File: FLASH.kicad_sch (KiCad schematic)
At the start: 0 parts

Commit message: added Buzzer, status LEDs
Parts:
- added C29: 100nF, Capacitor_SMD:C_0603_1608Metric, symbol Device:C
- added R12, R13, R14: 10k, Resistor_SMD:R_0603_1608Metric, symbol Device:R
- added U10: W25Q128JVSIQ, Package_SO:SOIC-8_5.3x5.3mm_P1.27mm, symbol Memory_Flash:W25Q128JVS
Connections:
- new net: R14.2, U10.3 (~{WP}/IO_{2})
- new net: R13.2, U10.7 (~{HOLD}/~{RESET}/IO_{3})
- new net 3V3: C29.1, R12.1, R13.1, R14.1, U10.8 (VCC)
- new net CLK_FLASH: U10.6 (CLK)
- new net CS_FLASH: R12.2, U10.1 (~{CS})
- new net DI_FLASH: U10.5 (DI/IO_{0})
- new net DO_FLASH: U10.2 (DO/IO_{1})
- new net GND: C29.2, U10.4 (GND)

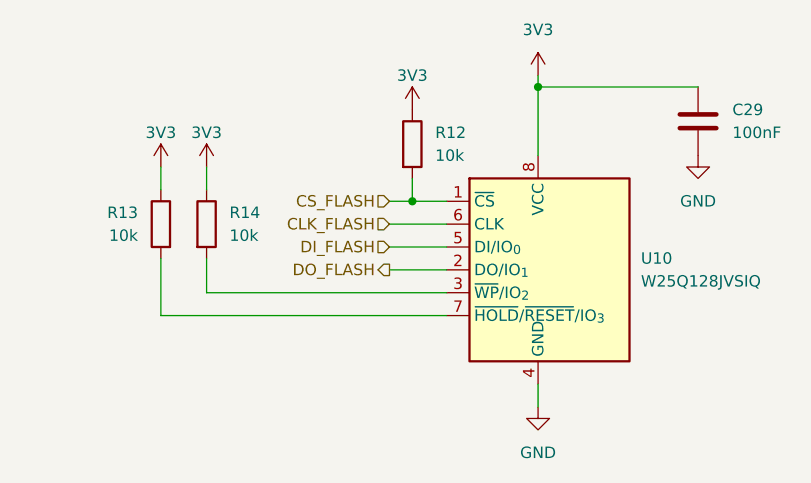
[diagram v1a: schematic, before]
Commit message: Battery protection, camera switch, 64MB flash, ERC clean
- Fuse + TVS on battery input, camera load switch (TPS22917)
- Flash to W25Q512JVFIQ (SOIC-16), hand-solder passive footprints
- Power LED, title blocks, U5 footprint, PWR/NC flags (0 ERC)
- Regenerated schematic PDF
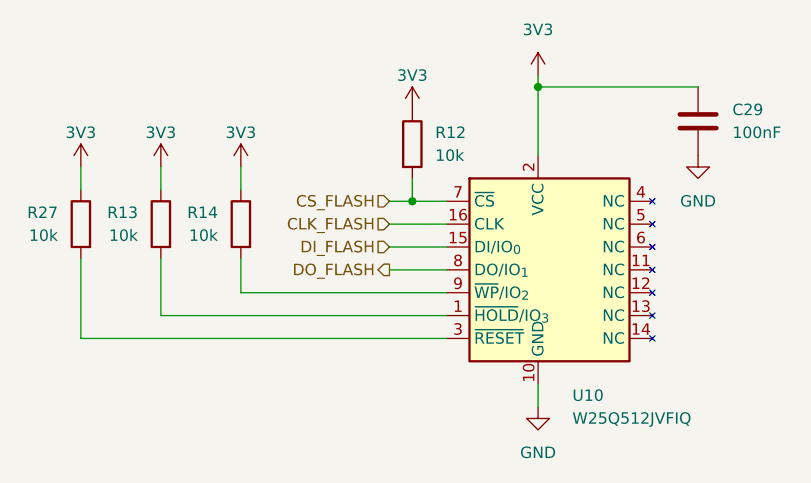
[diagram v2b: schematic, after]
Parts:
- added R27: 10k, Resistor_SMD:R_0603_1608Metric_Pad0.98x0.95mm_HandSolder, symbol Device:R
- C29: footprint Capacitor_SMD:C_0603_1608Metric -> Capacitor_SMD:C_0603_1608Metric_Pad1.08x0.95mm_HandSolder
- R12, R13, R14: footprint Resistor_SMD:R_0603_1608Metric -> Resistor_SMD:R_0603_1608Metric_Pad0.98x0.95mm_HandSolder
- U10: value W25Q128JVSIQ -> W25Q512JVFIQ; footprint Package_SO:SOIC-8_5.3x5.3mm_P1.27mm -> Package_SO:SOIC-16W_7.5x10.3mm_P1.27mm; symbol Memory_Flash:W25Q128JVS -> MyKiCAD:W25Q512JVFIQ
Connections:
- net 3V3: now also U10.2 (VCC), R27.1; no longer U10.8 (VCC)
- net CLK_FLASH: now also U10.16 (CLK); no longer U10.6 (CLK)
- net CS_FLASH: now also U10.7 (~{CS}); no longer U10.1 (~{CS})
- net DI_FLASH: now also U10.15 (DI/IO_{0}); no longer U10.5 (DI/IO_{0})
- net DO_FLASH: now also U10.8 (DO/IO_{1}); no longer U10.2 (DO/IO_{1})
- net GND: now also U10.10 (GND); no longer U10.4 (GND)
- net at U10.3 (~{RESET}): now also R27.2; no longer R14.2
- net at R13.2: now also U10.1 (~{HOLD}/IO_{3}); no longer U10.7 (~{HOLD}/~{RESET}/IO_{3})
- new net: R14.2, U10.9 (~{WP}/IO_{2})
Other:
- title: (none) -> Flight Data Flash
- moved on the sheet: R14
